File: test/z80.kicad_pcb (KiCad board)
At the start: 2 copper layers, 71.1 x 43.2 mm, 27 parts

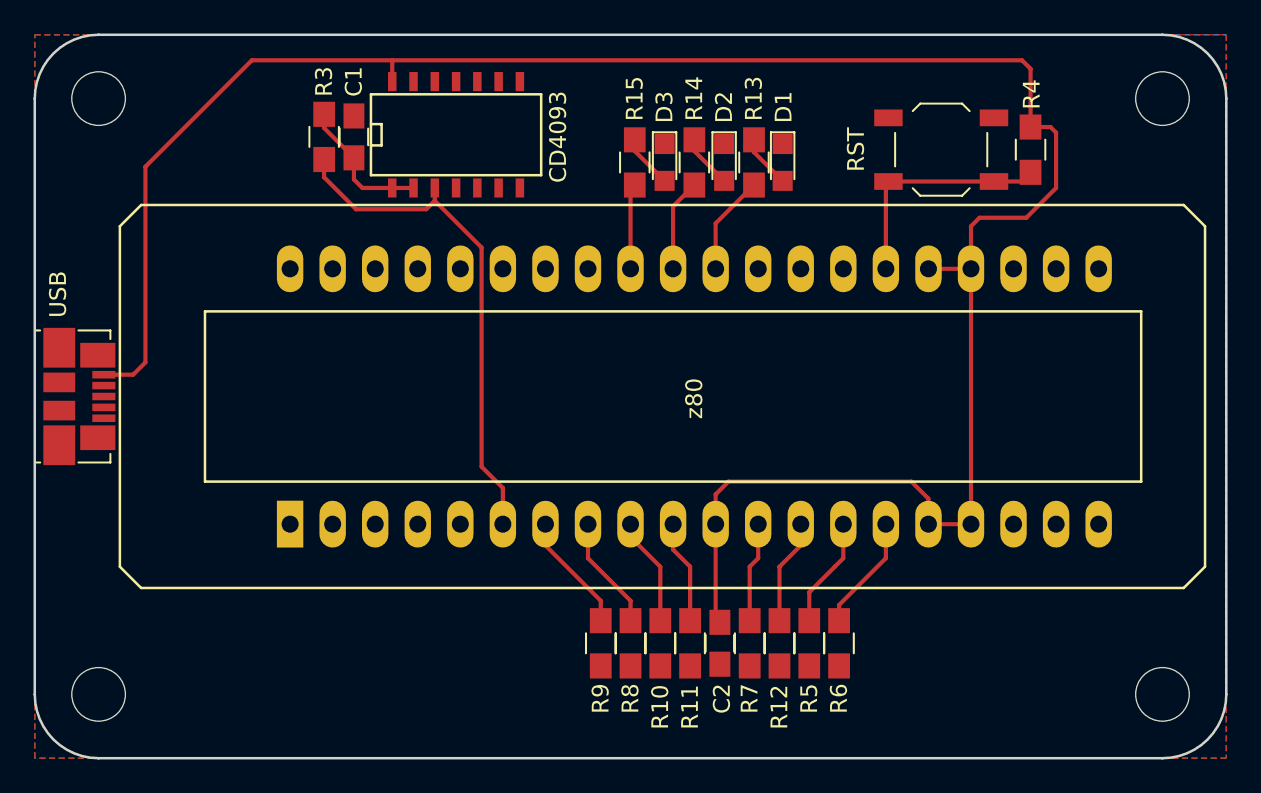
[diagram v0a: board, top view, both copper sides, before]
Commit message: Test board revision 2
- Replaced quad NAND gate with single NOT gate
- Broke out remaining address lines to LEDs
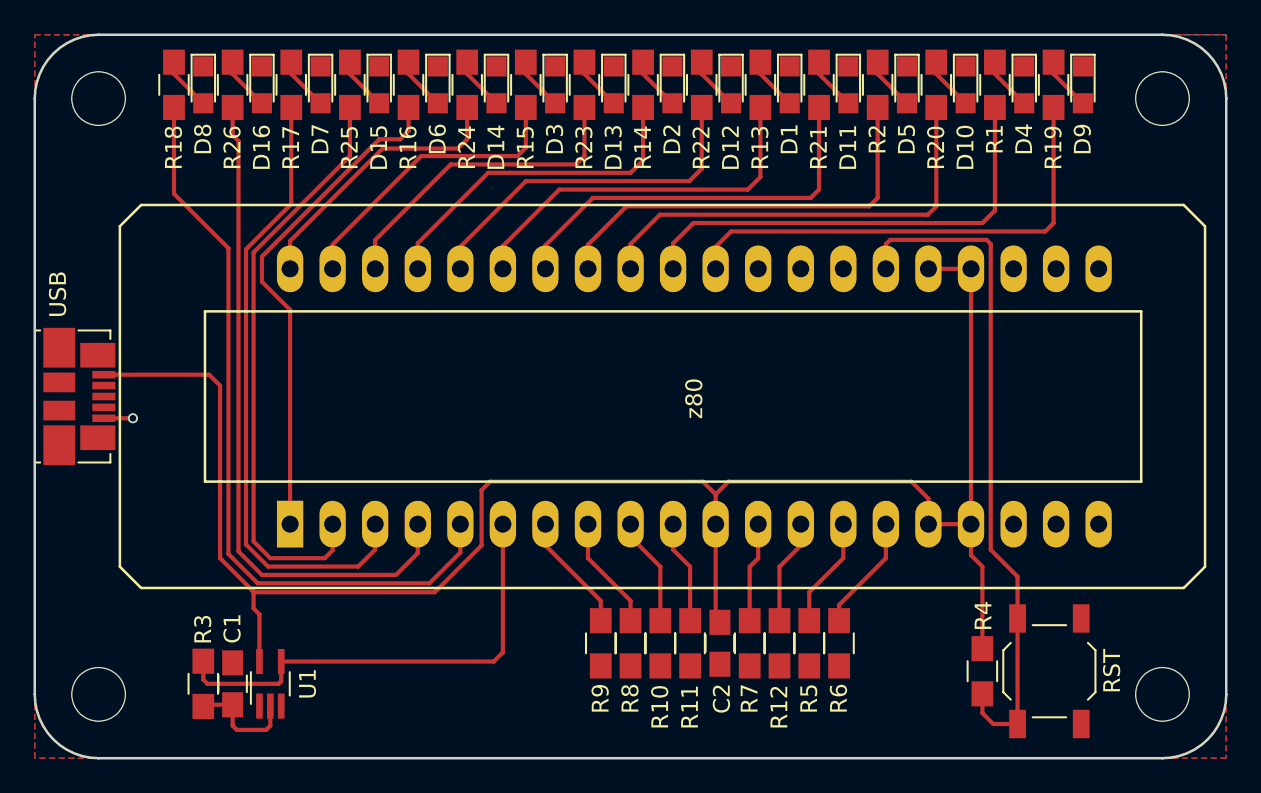
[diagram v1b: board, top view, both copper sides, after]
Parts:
- removed CD4093: 4093, SMD_Packages:SOIC-14_N
- added D10: LED, LEDs:LED_0805, F.Cu at (210.5, 83.0)
- added D11: LED, LEDs:LED_0805, F.Cu at (203.5, 83.0)
- added D12: LED, LEDs:LED_0805, F.Cu at (196.5, 83.0)
- added D13: LED, LEDs:LED_0805, F.Cu at (189.5, 83.0)
- added D14: LED, LEDs:LED_0805, F.Cu at (182.5, 83.0)
- added D15: LED, LEDs:LED_0805, F.Cu at (175.5, 83.0)
- added D16: LED, LEDs:LED_0805, F.Cu at (168.5, 83.0)
- added D4: LED, LEDs:LED_0805, F.Cu at (214.0, 83.0)
- added D5: LED, LEDs:LED_0805, F.Cu at (207.0, 83.0)
- added D6: LED, LEDs:LED_0805, F.Cu at (179.0, 83.0)
- added D7: LED, LEDs:LED_0805, F.Cu at (172.0, 83.0)
- added D8: LED, LEDs:LED_0805, F.Cu at (165.0, 83.0)
- added D9: LED, LEDs:LED_0805, F.Cu at (217.5, 83.0)
- added R1: 470R, Resistors_SMD:R_0805_HandSoldering, F.Cu at (212.2, 83.0)
- added R16: 470R, Resistors_SMD:R_0805_HandSoldering, F.Cu at (177.2, 83.0)
- added R17: 470R, Resistors_SMD:R_0805_HandSoldering, F.Cu at (170.2, 83.0)
- added R18: 470R, Resistors_SMD:R_0805_HandSoldering, F.Cu at (163.2, 83.0)
- added R19: 470R, Resistors_SMD:R_0805_HandSoldering, F.Cu at (215.8, 83.0)
- added R2: 470R, Resistors_SMD:R_0805_HandSoldering, F.Cu at (205.2, 83.0)
- added R20: 470R, Resistors_SMD:R_0805_HandSoldering, F.Cu at (208.8, 83.0)
- added R21: 470R, Resistors_SMD:R_0805_HandSoldering, F.Cu at (201.8, 83.0)
- added R22: 470R, Resistors_SMD:R_0805_HandSoldering, F.Cu at (194.8, 83.0)
- added R23: 470R, Resistors_SMD:R_0805_HandSoldering, F.Cu at (187.8, 83.0)
- added R24: 470R, Resistors_SMD:R_0805_HandSoldering, F.Cu at (180.8, 83.0)
- added R25: 470R, Resistors_SMD:R_0805_HandSoldering, F.Cu at (173.8, 83.0)
- added R26: 470R, Resistors_SMD:R_0805_HandSoldering, F.Cu at (166.8, 83.0)
- added U1: 74AHC1G14, TO_SOT_Packages_SMD:SOT-353_SC-70-5_Handsoldering, F.Cu at (169.0, 118.8)
- moved C1 33.4 mm to (166.8, 118.8)
- moved R3 33.4 mm to (165.0, 118.8), turned to 270 degrees
- moved RST1 31.8 mm to (215.5, 118.0), turned to 270 degrees
- moved R4 31.3 mm to (211.5, 118.0)
- moved D3 8.01 mm to (186.0, 83.0)
- moved R15 7.98 mm to (184.2, 83.0)
- moved D2 5.57 mm to (193.0, 83.0)
- moved R14 5.55 mm to (191.2, 83.0)
- moved D1 4.65 mm to (200.0, 83.0)
- moved R13 4.65 mm to (198.2, 83.0)
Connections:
- z80 pad 30: Net-(R13-Pad2) -> Net-(R19-Pad2)
- z80 pad 31: Net-(R14-Pad2) -> Net-(R1-Pad2)
- z80 pad 32: Net-(R15-Pad2) -> Net-(R20-Pad2)
- z80 pad 35: Net-(z80-Pad35) -> Net-(R13-Pad2)
- z80 pad 37: Net-(z80-Pad37) -> Net-(R14-Pad2)
- z80 pad 39: Net-(z80-Pad39) -> Net-(R15-Pad2)
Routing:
- net Net-(R18-Pad2): track 0.00 -> 45.0 mm
- net Net-(R26-Pad2): track 0.00 -> 40.2 mm
- net Net-(R17-Pad2): track 0.00 -> 37.4 mm
- net Net-(R25-Pad2): track 0.00 -> 35.2 mm
- net Net-(R16-Pad2): track 0.00 -> 29.9 mm
- net Net-(R19-Pad2): track 0.00 -> 29.0 mm
- net Net-(R1-Pad2): track 0.00 -> 27.9 mm
- net Net-(R20-Pad2): track 0.00 -> 26.8 mm
- net Net-(R4-Pad2): track 14.3 -> 40.8 mm
- net Net-(R2-Pad2): track 0.00 -> 25.3 mm
- net Net-(R21-Pad2): track 0.00 -> 24.0 mm
- net VCC: track 132.5 -> 109.1 mm
- net Net-(R22-Pad2): track 0.00 -> 21.3 mm
- net Net-(R23-Pad2): track 0.00 -> 19.2 mm
- net Net-(R24-Pad2): track 0.00 -> 16.6 mm
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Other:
- board text added: "Rev. 2"
- board text added: "Z80 CPU test circuit https://github.com/Wiles/z80"
- board text removed: "Rev. 1"
- board text removed: "Z80 CPU test circuit https://github.com/Wiles/z80 http://www.z80.info/z80test0.htm"

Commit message: Increase VCC track width
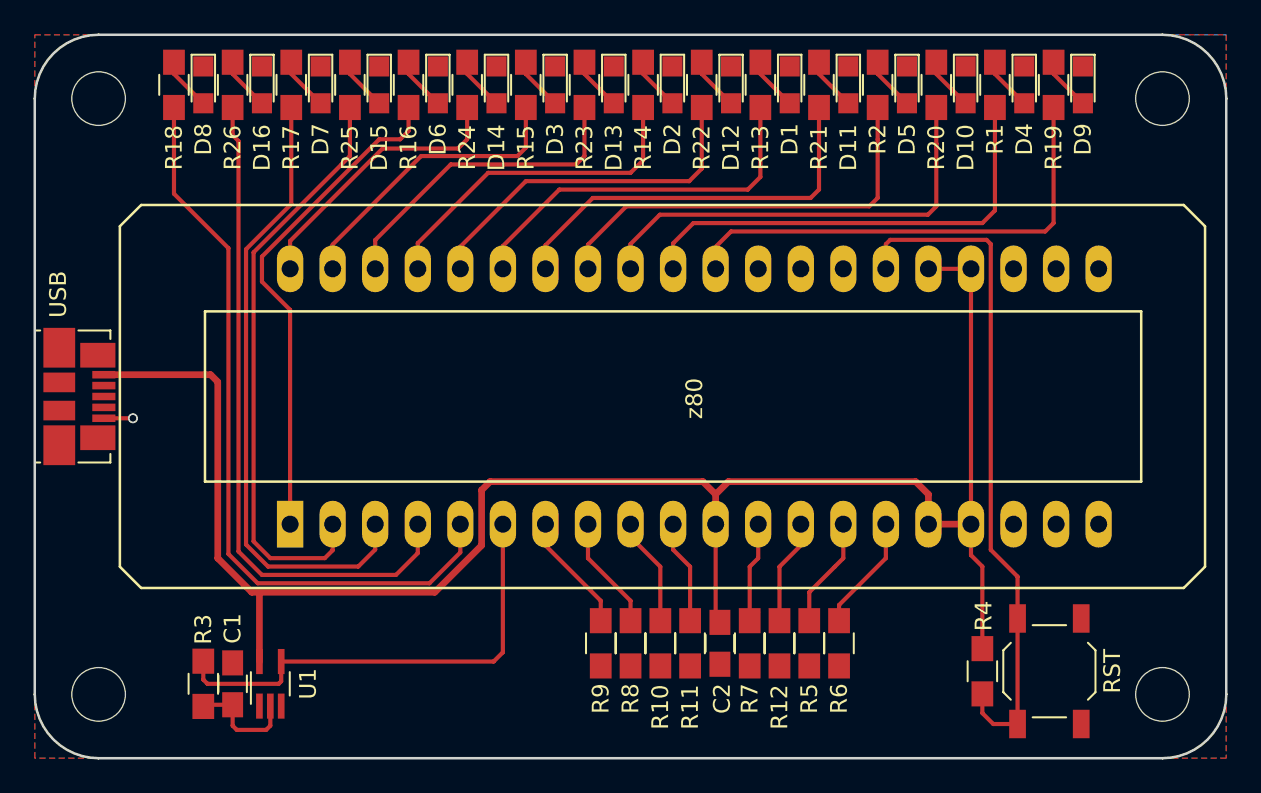
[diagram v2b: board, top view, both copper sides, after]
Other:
- net class VCC added: clearance 0.2, trace_width 0.4, via_dia 0.6, via_drill 0.4
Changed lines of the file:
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@@
     (links 86)
     (no_connects 0)
-    (area 154.864999 79.934999 226.135001 123.265001)
+    (area 149.192857 78.645 231.807143 124.655)
     (thickness 1.6)
     (drawings 10)
-    (tracks 216)
+    (tracks 213)
     (zones 0)
     (modules 53)
@@
     (add_net "Net-(z80-Pad27)")
     (add_net "Net-(z80-Pad28)")
+  )
+  (net_class VCC ""
+    (clearance 0.2)
+    (trace_width 0.4)
+    (via_dia 0.6)
+    (via_drill 0.4)
+    (uvia_dia 0.3)
+    (uvia_drill 0.1)
     (add_net VCC)
   )
@@
   (segment (start 166.75 120) (end 165.1 120) (width 0.25) (layer F.Cu) (net 1))
   (segment (start 165.1 120) (end 165 120.1) (width 0.25) (layer F.Cu) (net 1))
-  (segment (start 159.064 102.9) (end 160.8 102.9) (width 0.25) (layer F.Cu) (net 2) (status 400000))
+  (segment (start 159.064 102.9) (end 160.8 102.9) (width 0.25) (layer F.Cu) (net 2))
   (via (at 160.8 102.9) (size 0.6) (drill 0.4) (layers F.Cu B.Cu) (net 2))
-  (segment (start 195.58 109.22) (end 195.58 107.442) (width 0.25) (layer F.Cu) (net 3) (status 400000))
-  (segment (start 195.58 107.442) (end 194.818 106.68) (width 0.25) (layer F.Cu) (net 3))
-  (segment (start 167.950002 113.234002) (end 167.950002 113.200002) (width 0.25) (layer F.Cu) (net 3))
-  (segment (start 168 113.284) (end 167.950002 113.234002) (width 0.25) (layer F.Cu) (net 3))
-  (segment (start 178.816 113.284) (end 168 113.284) (width 0.25) (layer F.Cu) (net 3))
-  (segment (start 181.61 110.49) (end 178.816 113.284) (width 0.25) (layer F.Cu) (net 3))
-  (segment (start 181.61 107.188) (end 181.61 110.49) (width 0.25) (layer F.Cu) (net 3))
-  (segment (start 182.118 106.68) (end 181.61 107.188) (width 0.25) (layer F.Cu) (net 3))
-  (segment (start 194.818 106.68) (end 182.118 106.68) (width 0.25) (layer F.Cu) (net 3))
-  (segment (start 210.82 109.22) (end 208.28 109.22) (width 0.25) (layer F.Cu) (net 3))
-  (segment (start 168 113.200002) (end 168 114.25) (width 0.25) (layer F.Cu) (net 3))
-  (segment (start 168.35 114.6) (end 168.35 117.42) (width 0.25) (layer F.Cu) (net 3))
-  (segment (start 168 114.25) (end 168.35 114.6) (width 0.25) (layer F.Cu) (net 3))
-  (segment (start 159.064 100.3) (end 165.349998 100.3) (width 0.25) (layer F.Cu) (net 3))
-  (segment (start 167.950002 113.200002) (end 168 113.200002) (width 0.25) (layer F.Cu) (net 3))
-  (segment (start 166 111.25) (end 167.950002 113.200002) (width 0.25) (layer F.Cu) (net 3))
-  (segment (start 166 100.950002) (end 166 111.25) (width 0.25) (layer F.Cu) (net 3))
-  (segment (start 165.349998 100.3) (end 166 100.950002) (width 0.25) (layer F.Cu) (net 3))
+  (segment (start 208.28 109.22) (end 210.82 109.22) (width 0.4) (layer F.Cu) (net 3))
+  (segment (start 195.58 107.442) (end 196.342 106.68) (width 0.4) (layer F.Cu) (net 3))
+  (segment (start 208.28 107.442) (end 208.28 109.22) (width 0.4) (layer F.Cu) (net 3))
+  (segment (start 207.518 106.68) (end 208.28 107.442) (width 0.4) (layer F.Cu) (net 3))
+  (segment (start 196.342 106.68) (end 207.518 106.68) (width 0.4) (layer F.Cu) (net 3))
+  (segment (start 194.818 106.68) (end 195.58 107.442) (width 0.4) (layer F.Cu) (net 3))
+  (segment (start 168.402 113.284) (end 178.816 113.284) (width 0.4) (layer F.Cu) (net 3))
+  (segment (start 178.816 113.284) (end 181.61 110.49) (width 0.4) (layer F.Cu) (net 3))
+  (segment (start 181.61 110.49) (end 181.61 107.188) (width 0.4) (layer F.Cu) (net 3))
+  (segment (start 181.61 107.188) (end 182.118 106.68) (width 0.4) (layer F.Cu) (net 3))
+  (segment (start 182.118 106.68) (end 194.818 106.68) (width 0.4) (layer F.Cu) (net 3))
+  (segment (start 195.58 107.442) (end 195.58 109.22) (width 0.4) (layer F.Cu) (net 3))
+  (segment (start 168.35 117.42) (end 168.35 113.284) (width 0.4) (layer F.Cu) (net 3))
+  (segment (start 168.35 113.284) (end 168.402 113.284) (width 0.4) (layer F.Cu) (net 3))
+  (segment (start 159.064 100.3) (end 165.436998 100.3) (width 0.4) (layer F.Cu) (net 3))
+  (segment (start 167.894 113.284) (end 168.402 113.284) (width 0.4) (layer F.Cu) (net 3))
+  (segment (start 165.862 111.252) (end 167.894 113.284) (width 0.4) (layer F.Cu) (net 3))
+  (segment (start 165.862 100.725002) (end 165.862 111.252) (width 0.4) (layer F.Cu) (net 3))
+  (segment (start 165.436998 100.3) (end 165.862 100.725002) (width 0.4) (layer F.Cu) (net 3))
   (segment (start 210.82 109.22) (end 210.82 111.07) (width 0.25) (layer F.Cu) (net 3))
+  (segment (start 210.82 111.07) (end 211.5 111.75) (width 0.25) (layer F.Cu) (net 3))
   (segment (start 211.5 111.75) (end 211.5 116.65) (width 0.25) (layer F.Cu) (net 3))
-  (segment (start 210.82 111.07) (end 211.5 111.75) (width 0.25) (layer F.Cu) (net 3))
-  (segment (start 208.28 109.22) (end 208.28 107.696) (width 0.25) (layer F.Cu) (net 3))
-  (segment (start 196.342 106.68) (end 195.58 107.442) (width 0.25) (layer F.Cu) (net 3))
-  (segment (start 207.264 106.68) (end 196.342 106.68) (width 0.25) (layer F.Cu) (net 3))
-  (segment (start 208.28 107.696) (end 207.264 106.68) (width 0.25) (layer F.Cu) (net 3))
   (segment (start 195.58 108.204) (end 195.58 109.22) (width 0.25) (layer F.Cu) (net 3))
   (segment (start 195.58 109.22) (end 195.58 114.828) (width 0.25) (layer F.Cu) (net 3))

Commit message: Moved reset button label
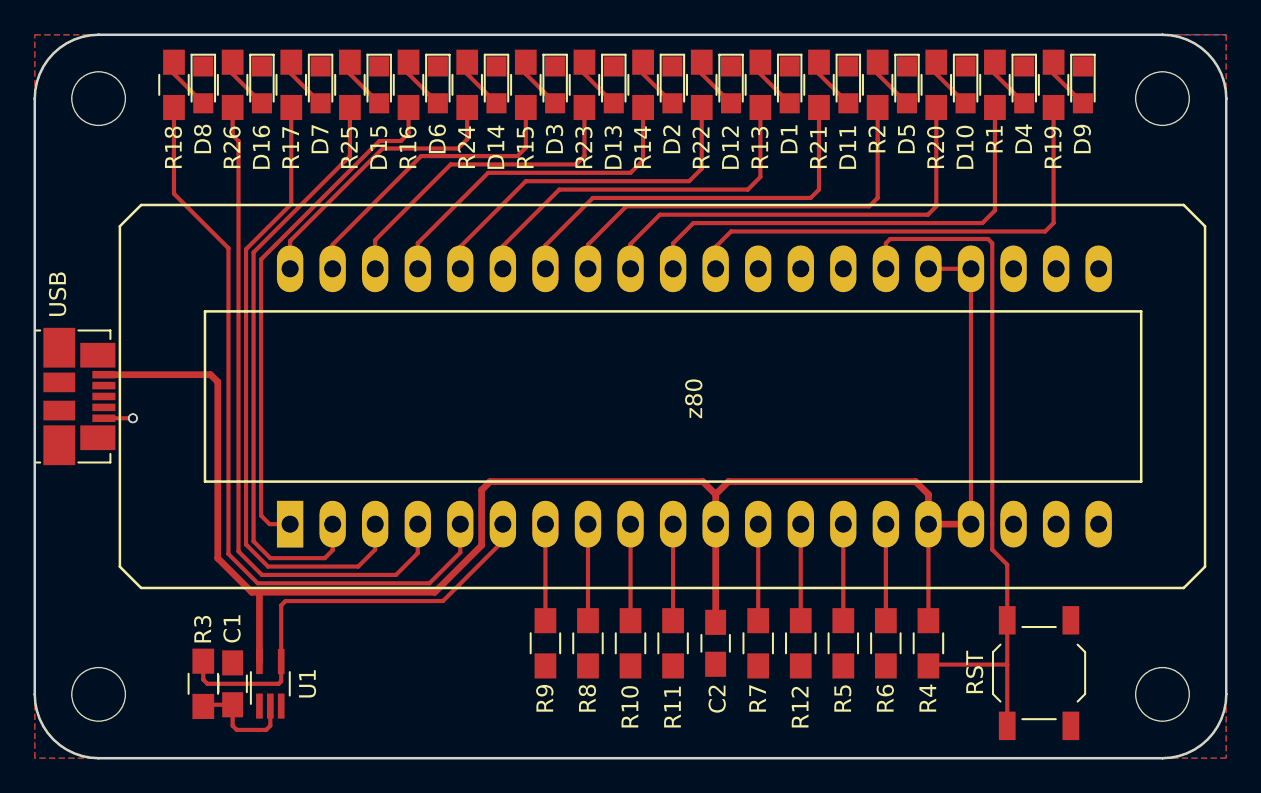
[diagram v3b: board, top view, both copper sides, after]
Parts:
- moved R4 3.63 mm to (208.3, 116.3)
- moved R9 3.30 mm to (185.4, 116.3)
- moved R6 2.79 mm to (205.7, 116.3)
- moved R8 2.54 mm to (188.0, 116.3)
- moved R5 2.03 mm to (203.2, 116.3)
- moved R10 1.78 mm to (190.5, 116.3)
- moved R12 1.27 mm to (200.7, 116.3)
- moved R11 1.02 mm to (193.0, 116.3)
- moved RST1 0.63 mm to (214.9, 118.1)
- moved R7 0.51 mm to (198.1, 116.3)
- moved C2 0.25 mm to (195.6, 116.3)
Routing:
- net Net-(R3-Pad1): track 29.2 -> 27.3 mm
- net VCC: track 109.1 -> 107.4 mm
- net Net-(R4-Pad2): track 40.8 -> 42.0 mm
- net Net-(R6-Pad2): track 6.92 -> 5.76 mm
- net Net-(R8-Pad2): track 6.81 -> 5.76 mm
- net Net-(R5-Pad2): track 7.11 -> 6.27 mm
- net Net-(R16-Pad2): track 29.9 -> 30.7 mm
- net Net-(R12-Pad2): track 6.29 -> 7.03 mm
